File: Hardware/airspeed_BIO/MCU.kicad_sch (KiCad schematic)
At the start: 10 parts, among them SW1 434123025826, U4 STM32F042G6Ux, Y1 830108313809

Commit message: set Ilimit and set footprint
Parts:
- C21, C22, C23, C24, C25: footprint Capacitor_SMD:C_0402_1005Metric -> Capacitor_SMD:C_0603_1608Metric
- R24, R25: footprint Resistor_SMD:R_0402_1005Metric -> Resistor_SMD:R_0603_1608Metric
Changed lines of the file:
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@@
 			)
 		)
-		(property "Footprint" "Capacitor_SMD:C_0402_1005Metric"
+		(property "Footprint" "Capacitor_SMD:C_0603_1608Metric"
 			(at 58.42 106.68 0)
 			(effects
@@
 			)
 		)
-		(property "Footprint" "Capacitor_SMD:C_0402_1005Metric"
+		(property "Footprint" "Capacitor_SMD:C_0603_1608Metric"
 			(at 143.51 60.96 0)
 			(effects
@@
 			)
 		)
-		(property "Footprint" "Capacitor_SMD:C_0402_1005Metric"
+		(property "Footprint" "Capacitor_SMD:C_0603_1608Metric"
 			(at 130.81 60.96 0)
 			(effects
@@
 			)
 		)
-		(property "Footprint" "Capacitor_SMD:C_0402_1005Metric"
+		(property "Footprint" "Capacitor_SMD:C_0603_1608Metric"
 			(at 81.28 68.58 0)
 			(effects
@@
 			)
 		)
-		(property "Footprint" "Capacitor_SMD:C_0402_1005Metric"
+		(property "Footprint" "Capacitor_SMD:C_0603_1608Metric"
 			(at 58.42 93.98 0)
 			(effects
@@
 			)
 		)
-		(property "Footprint" "Resistor_SMD:R_0402_1005Metric"
+		(property "Footprint" "Resistor_SMD:R_0603_1608Metric"
 			(at 74.93 106.68 0)
 			(effects
@@
 	)
 	(symbol
+		(lib_name "R_Small_1")
 		(lib_id "Device:R_Small")
 		(at 81.28 58.42 180)
@@
 			)
 		)
-		(property "Footprint" "Resistor_SMD:R_0402_1005Metric"
+		(property "Footprint" "Resistor_SMD:R_0603_1608Metric"
 			(at 81.28 58.42 0)
 			(effects

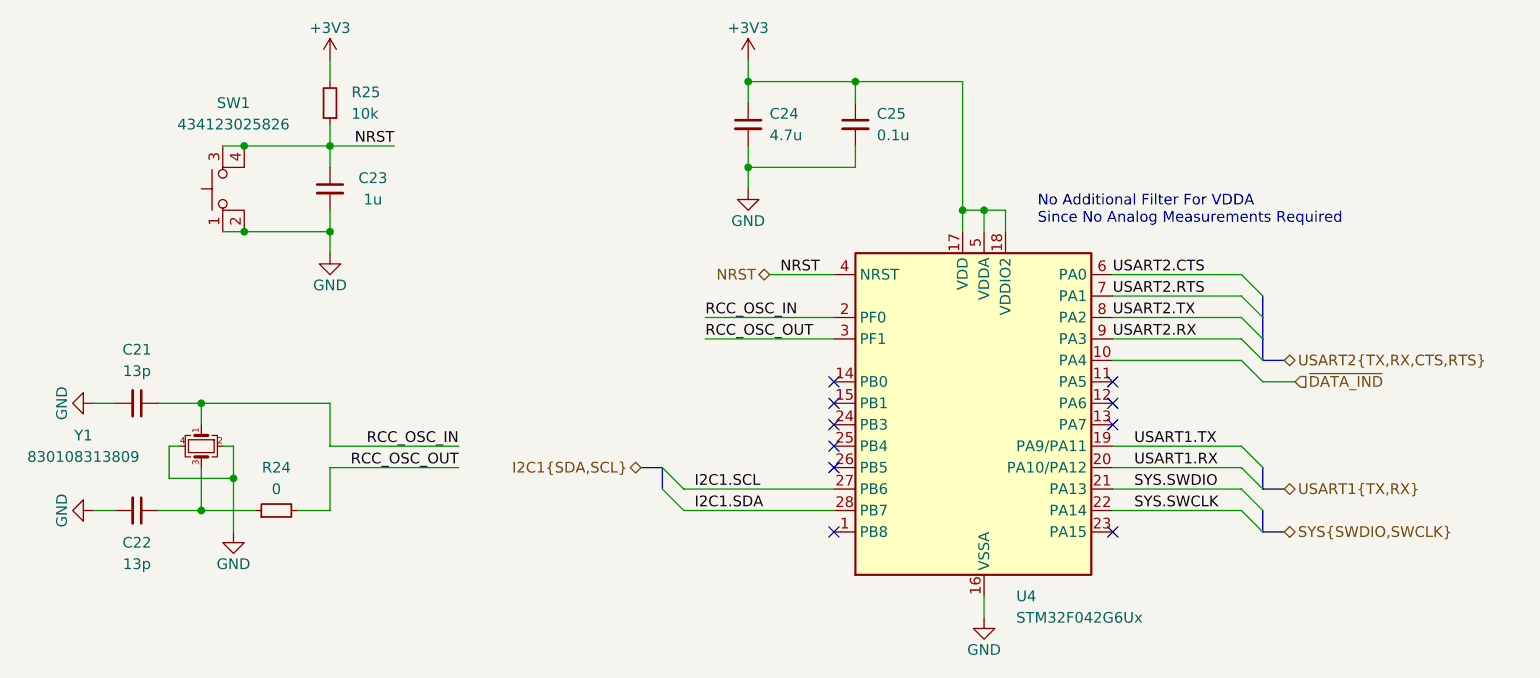
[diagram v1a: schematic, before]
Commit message: layout and fix Schematic
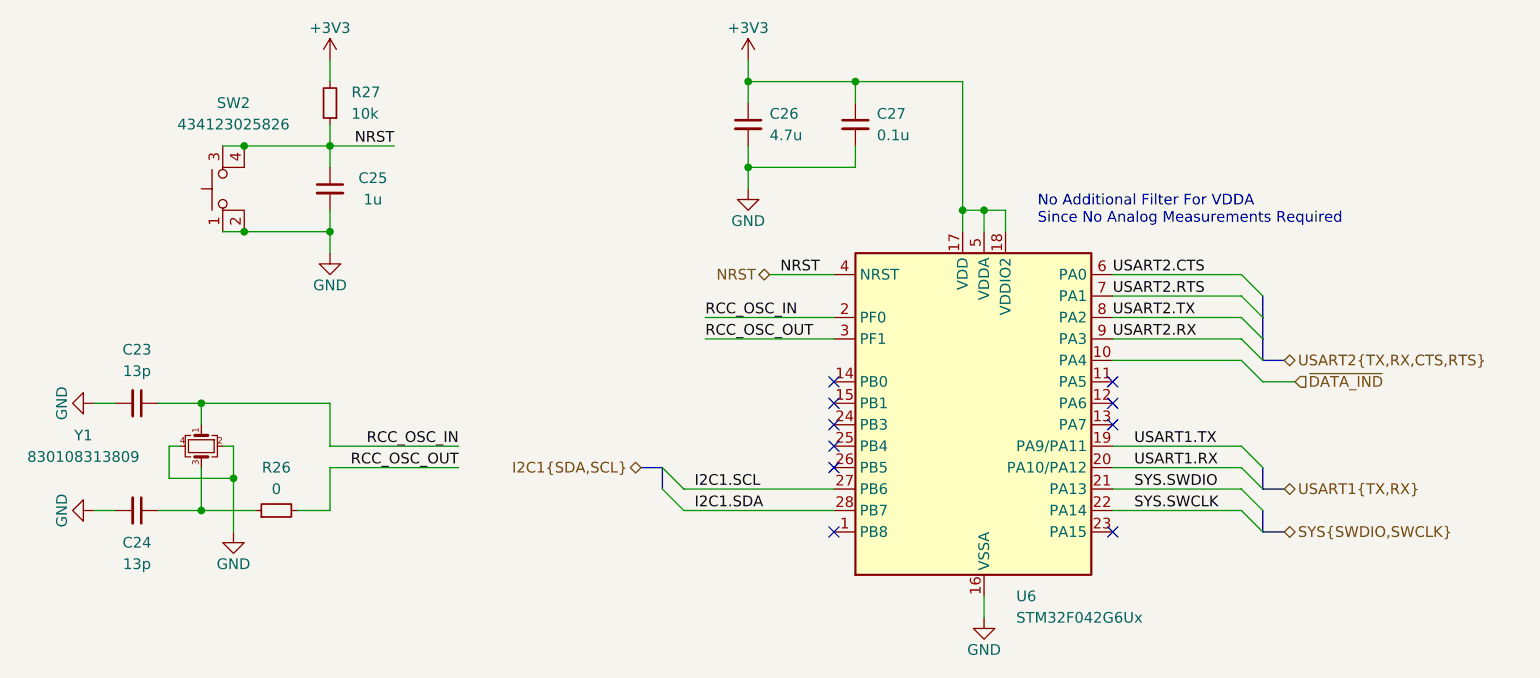
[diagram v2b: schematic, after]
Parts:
- renumbered C21 to C23, C22 to C24, C23 to C25, C24 to C26, C25 to C27, R24 to R26, R25 to R27, SW1 to SW2, U4 to U6
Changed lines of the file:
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@@
 		(on_board yes)
 		(dnp no)
-		(property "Reference" "C22"
+		(property "Reference" "C24"
 			(at 58.42 110.49 90)
 			(effects
@@
 			(project "airspeed_BIO"
 				(path "/6ddcf4fe-9e51-4114-8222-5fc3f810c12a/ac3ccc3e-0bab-47ba-8bac-2fd6453dfecf"
-					(reference "C22")
+					(reference "C24")
 					(unit 1)
 				)
@@
 		(on_board yes)
 		(dnp no)
-		(property "Reference" "#PWR030"
+		(property "Reference" "#PWR039"
 			(at 81.28 57.15 0)
 			(effects
@@
 			(project "airspeed_BIO"
 				(path "/6ddcf4fe-9e51-4114-8222-5fc3f810c12a/ac3ccc3e-0bab-47ba-8bac-2fd6453dfecf"
-					(reference "#PWR030")
+					(reference "#PWR039")
 					(unit 1)
 				)
@@
 		(on_board yes)
 		(dnp no)
-		(property "Reference" "#PWR027"
+		(property "Reference" "#PWR036"
 			(at 46.99 93.98 0)
 			(effects
@@
 			(project "airspeed_BIO"
 				(path "/6ddcf4fe-9e51-4114-8222-5fc3f810c12a/ac3ccc3e-0bab-47ba-8bac-2fd6453dfecf"
-					(reference "#PWR027")
+					(reference "#PWR036")
 					(unit 1)
 				)
@@
 		(on_board yes)
 		(dnp no)
-		(property "Reference" "SW1"
+		(property "Reference" "SW2"
 			(at 69.85 58.42 90)
 			(effects
@@
 			(project "airspeed_BIO"
 				(path "/6ddcf4fe-9e51-4114-8222-5fc3f810c12a/ac3ccc3e-0bab-47ba-8bac-2fd6453dfecf"
-					(reference "SW1")
+					(reference "SW2")
 					(unit 1)
 				)
@@
 		(on_board yes)
 		(dnp no)
-		(property "Reference" "U4"
+		(property "Reference" "U6"
 			(at 162.56 116.84 0)
 			(effects
@@
 			(project "airspeed_BIO"
 				(path "/6ddcf4fe-9e51-4114-8222-5fc3f810c12a/ac3ccc3e-0bab-47ba-8bac-2fd6453dfecf"
-					(reference "U4")
+					(reference "U6")
 					(unit 1)
 				)
@@
 		(dnp no)
 		(fields_autoplaced yes)
-		(property "Reference" "C25"
+		(property "Reference" "C27"
 			(at 146.05 59.6962 0)
 			(effects
@@
 			(project "airspeed_BIO"
 				(path "/6ddcf4fe-9e51-4114-8222-5fc3f810c12a/ac3ccc3e-0bab-47ba-8bac-2fd6453dfecf"
-					(reference "C25")
+					(reference "C27")
 					(unit 1)
 				)
@@
 		(on_board yes)
 		(dnp no)
-		(property "Reference" "C24"
+		(property "Reference" "C26"
 			(at 133.35 59.69 0)
 			(effects
@@
 			(project "airspeed_BIO"
 				(path "/6ddcf4fe-9e51-4114-8222-5fc3f810c12a/ac3ccc3e-0bab-47ba-8bac-2fd6453dfecf"
-					(reference "C24")
+					(reference "C26")
 					(unit 1)
 				)
@@
 		(on_board yes)
 		(dnp no)
-		(property "Reference" "#PWR029"
+		(property "Reference" "#PWR038"
 			(at 69.85 115.57 0)
 			(effects
@@
 			(project "airspeed_BIO"
 				(path "/6ddcf4fe-9e51-4114-8222-5fc3f810c12a/ac3ccc3e-0bab-47ba-8bac-2fd6453dfecf"
-					(reference "#PWR029")
+					(reference "#PWR038")
 					(unit 1)
 				)
@@
 		(on_board yes)
 		(dnp no)
-		(property "Reference" "C23"
+		(property "Reference" "C25"
 			(at 86.36 67.31 0)
 			(effects
@@
 			(project "airspeed_BIO"
 				(path "/6ddcf4fe-9e51-4114-8222-5fc3f810c12a/ac3ccc3e-0bab-47ba-8bac-2fd6453dfecf"
-					(reference "C23")
+					(reference "C25")
 					(unit 1)
 				)
@@
 		(on_board yes)
 		(dnp no)
-		(property "Reference" "#PWR031"
+		(property "Reference" "#PWR040"
 			(at 81.28 82.55 0)
 			(effects
@@
 			(project "airspeed_BIO"
 				(path "/6ddcf4fe-9e51-4114-8222-5fc3f810c12a/ac3ccc3e-0bab-47ba-8bac-2fd6453dfecf"
-					(reference "#PWR031")
+					(reference "#PWR040")
 					(unit 1)
 				)
@@
 		(on_board yes)
 		(dnp no)
-		(property "Reference" "C21"
+		(property "Reference" "C23"
 			(at 58.42 87.63 90)
 			(effects
@@
 			(project "airspeed_BIO"
 				(path "/6ddcf4fe-9e51-4114-8222-5fc3f810c12a/ac3ccc3e-0bab-47ba-8bac-2fd6453dfecf"
-					(reference "C21")
+					(reference "C23")
 					(unit 1)
 				)
@@
 		(dnp no)
 		(fields_autoplaced yes)
-		(property "Reference" "R24"
+		(property "Reference" "R26"
 			(at 74.93 101.6 90)
 			(effects
@@
 			(project "airspeed_BIO"
 				(path "/6ddcf4fe-9e51-4114-8222-5fc3f810c12a/ac3ccc3e-0bab-47ba-8bac-2fd6453dfecf"
-					(reference "R24")
+					(reference "R26")
 					(unit 1)
 				)
@@
 		(dnp no)
 		(fields_autoplaced yes)
-		(property "Reference" "R25"
+		(property "Reference" "R27"
 			(at 83.82 57.15 0)
 			(effects
@@
 			(project "airspeed_BIO"
 				(path "/6ddcf4fe-9e51-4114-8222-5fc3f810c12a/ac3ccc3e-0bab-47ba-8bac-2fd6453dfecf"
-					(reference "R25")
+					(reference "R27")
 					(unit 1)
 				)
@@
 		(on_board yes)
 		(dnp no)
-		(property "Reference" "#PWR034"
+		(property "Reference" "#PWR043"
 			(at 158.75 125.73 0)
 			(effects
@@
 			(project "airspeed_BIO"
 				(path "/6ddcf4fe-9e51-4114-8222-5fc3f810c12a/ac3ccc3e-0bab-47ba-8bac-2fd6453dfecf"
-					(reference "#PWR034")
+					(reference "#PWR043")
 					(unit 1)
 				)
@@
 		(on_board yes)
 		(dnp no)
-		(property "Reference" "#PWR028"
+		(property "Reference" "#PWR037"
 			(at 46.99 106.68 0)
 			(effects
@@
 			(project "airspeed_BIO"
 				(path "/6ddcf4fe-9e51-4114-8222-5fc3f810c12a/ac3ccc3e-0bab-47ba-8bac-2fd6453dfecf"
-					(reference "#PWR028")
+					(reference "#PWR037")
 					(unit 1)
 				)
@@
 		(on_board yes)
 		(dnp no)
-		(property "Reference" "#PWR032"
+		(property "Reference" "#PWR041"
 			(at 130.81 57.15 0)
 			(effects
@@
 			(project "airspeed_BIO"
 				(path "/6ddcf4fe-9e51-4114-8222-5fc3f810c12a/ac3ccc3e-0bab-47ba-8bac-2fd6453dfecf"
-					(reference "#PWR032")
+					(reference "#PWR041")
 					(unit 1)
 				)
@@
 		(on_board yes)
 		(dnp no)
-		(property "Reference" "#PWR033"
+		(property "Reference" "#PWR042"
 			(at 130.81 74.93 0)
 			(effects
@@
 			(project "airspeed_BIO"
 				(path "/6ddcf4fe-9e51-4114-8222-5fc3f810c12a/ac3ccc3e-0bab-47ba-8bac-2fd6453dfecf"
-					(reference "#PWR033")
-					(unit 1)
-				)
+					(reference "#PWR042")
+					(unit 1)
+				)

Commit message: layoyt end
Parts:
- renumbered C23 to C22, C24 to C23, C25 to C24, C26 to C25, C27 to C26
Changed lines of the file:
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@@
 		(on_board yes)
 		(dnp no)
-		(property "Reference" "C24"
+		(property "Reference" "C23"
 			(at 58.42 110.49 90)
 			(effects
@@
 			(project "airspeed_BIO"
 				(path "/6ddcf4fe-9e51-4114-8222-5fc3f810c12a/ac3ccc3e-0bab-47ba-8bac-2fd6453dfecf"
-					(reference "C24")
+					(reference "C23")
 					(unit 1)
 				)
@@
 		(dnp no)
 		(fields_autoplaced yes)
-		(property "Reference" "C27"
+		(property "Reference" "C26"
 			(at 146.05 59.6962 0)
 			(effects
@@
 			(project "airspeed_BIO"
 				(path "/6ddcf4fe-9e51-4114-8222-5fc3f810c12a/ac3ccc3e-0bab-47ba-8bac-2fd6453dfecf"
-					(reference "C27")
+					(reference "C26")
 					(unit 1)
 				)
@@
 		(on_board yes)
 		(dnp no)
-		(property "Reference" "C26"
+		(property "Reference" "C25"
 			(at 133.35 59.69 0)
 			(effects
@@
 			(project "airspeed_BIO"
 				(path "/6ddcf4fe-9e51-4114-8222-5fc3f810c12a/ac3ccc3e-0bab-47ba-8bac-2fd6453dfecf"
-					(reference "C26")
+					(reference "C25")
 					(unit 1)
 				)
@@
 		(on_board yes)
 		(dnp no)
-		(property "Reference" "C25"
+		(property "Reference" "C24"
 			(at 86.36 67.31 0)
 			(effects
@@
 			(project "airspeed_BIO"
 				(path "/6ddcf4fe-9e51-4114-8222-5fc3f810c12a/ac3ccc3e-0bab-47ba-8bac-2fd6453dfecf"
-					(reference "C25")
+					(reference "C24")
 					(unit 1)
 				)
@@
 		(on_board yes)
 		(dnp no)
-		(property "Reference" "C23"
+		(property "Reference" "C22"
 			(at 58.42 87.63 90)
 			(effects
@@
 			(project "airspeed_BIO"
 				(path "/6ddcf4fe-9e51-4114-8222-5fc3f810c12a/ac3ccc3e-0bab-47ba-8bac-2fd6453dfecf"
-					(reference "C23")
-					(unit 1)
-				)
+					(reference "C22")
+					(unit 1)
+				)
